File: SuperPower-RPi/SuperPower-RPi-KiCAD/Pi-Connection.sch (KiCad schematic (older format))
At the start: 1 part, among them J1 Raspberry_Pi_2_3

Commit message: Cleaned up documentation.
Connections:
- no-connect marks 21 -> 24
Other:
- note added: "Pins to STM32:\nGPIO5 to trigger update\nGPIO4 to indicate reboot/restart"
- note removed: "Pins to STM32:\nGPIO____ to trigger update\nGPIO____ to indicate reboot/restart"
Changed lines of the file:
@@
 NoConn ~ 6000 2300
 Text Notes 1200 2500 0    50   ~ 0
-Pins to STM32:\nGPIO____ to trigger update\nGPIO____ to indicate reboot/restart
+Pins to STM32:\nGPIO5 to trigger update\nGPIO4 to indicate reboot/restart
 Text HLabel 6800 3300 2    50   BiDi ~ 0
 GPIO4
@@
 Wire Wire Line
 	5000 4100 4700 4100
+NoConn ~ 5000 3800
+NoConn ~ 5000 3900
+NoConn ~ 5000 4000
 $EndSCHEMATC

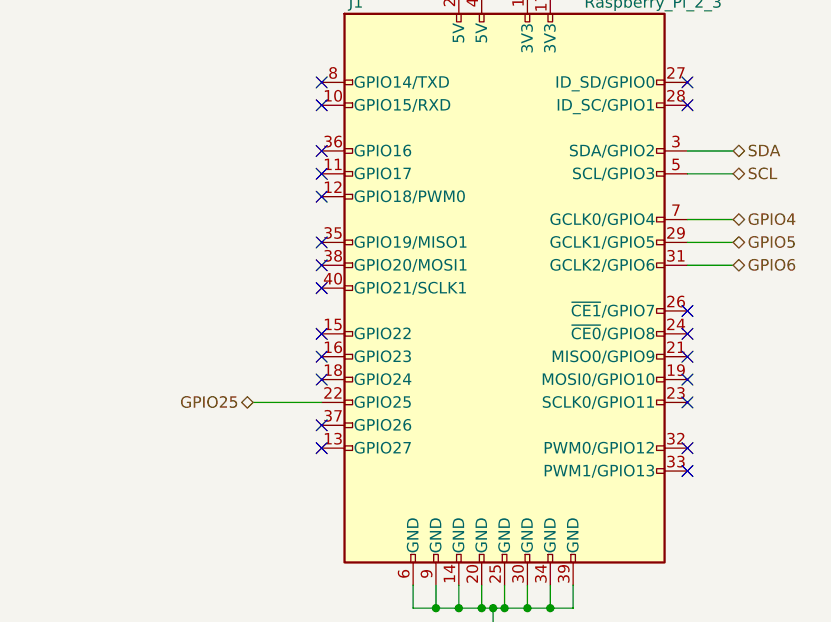
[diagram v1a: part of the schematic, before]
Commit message: Split the I2C busses and added the RPi-SWD connection.
It was found that when the RPi was powered off, the I2C connection was lost.
This was because the RPI has pull-ups on board that would act as voltage dividers.

The SWD connection to the RPi was made via jumpers to allow programming and
debugging of the STM directly via the Pi.
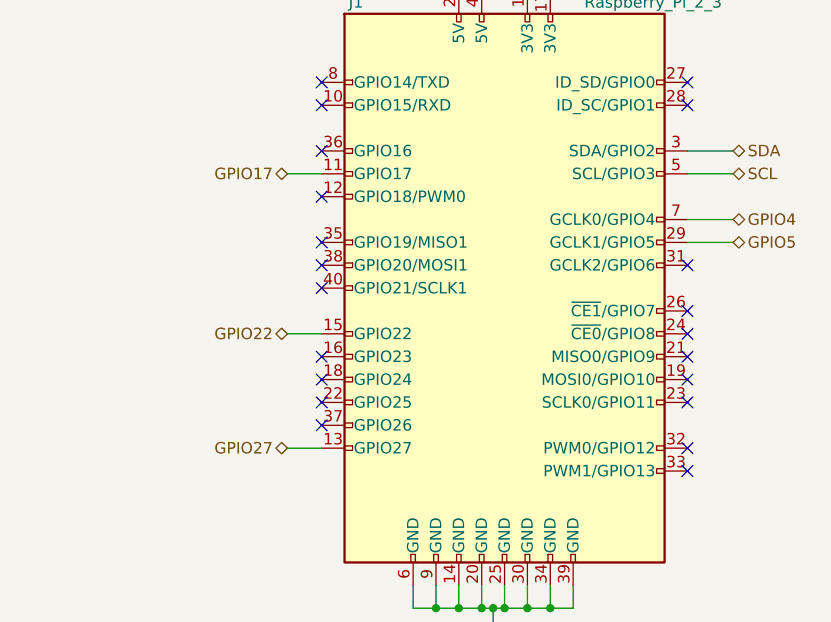
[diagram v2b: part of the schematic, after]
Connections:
- net GPIO17: now reaches J1.11 (GPIO17)
- net GPIO27: now reaches J1.13 (GPIO27)
- net GPIO22: now reaches J1.15 (GPIO22)
- net GPIO25: no longer names the net of J1.22 (GPIO25)
- net GPIO6: no longer names the net of J1.31 (GCLK2/GPIO6)
- no-connect marks 24 -> 23
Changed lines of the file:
@@
 NoConn ~ 5000 2800
 NoConn ~ 5000 3000
-NoConn ~ 5000 3100
 NoConn ~ 5000 3200
 NoConn ~ 5000 3400
@@
 NoConn ~ 5000 3600
 NoConn ~ 5000 4200
-NoConn ~ 5000 4300
 $Comp
 L power:GND #PWR09
@@
 Text HLabel 6800 3400 2    50   BiDi ~ 0
 GPIO5
-Text HLabel 6800 3500 2    50   BiDi ~ 0
-GPIO6
-Text HLabel 4700 4100 0    50   BiDi ~ 0
-GPIO25
 Wire Wire Line
 	6800 3400 6600 3400
-Wire Wire Line
-	6800 3500 6600 3500
-Wire Wire Line
-	5000 4100 4700 4100
-NoConn ~ 5000 3800
 NoConn ~ 5000 3900
 NoConn ~ 5000 4000
+NoConn ~ 5000 4100
+NoConn ~ 6600 3500
+Text HLabel 4850 3100 0    50   BiDi ~ 0
+GPIO17
+Wire Wire Line
+	4850 3100 5000 3100
+Text HLabel 4850 4300 0    50   BiDi ~ 0
+GPIO27
+Wire Wire Line
+	4850 4300 5000 4300
+Text HLabel 4850 3800 0    50   BiDi ~ 0
+GPIO22
+Wire Wire Line
+	4850 3800 5000 3800
 $EndSCHEMATC

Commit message: Updated schematic to fill out all BOM entries.
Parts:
- J1: Mfg (none) -> DNP
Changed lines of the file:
@@
 F 2 "Connector_PinSocket_2.54mm:PinSocket_2x20_P2.54mm_Vertical" H 5800 3600 50  0001 C CNN
 F 3 "https://www.raspberrypi.org/documentation/hardware/raspberrypi/schematics/rpi_SCH_3bplus_1p0_reduced.pdf" H 5800 3600 50  0001 C CNN
+F 4 "DNP" H 5800 3600 50  0001 C CNN "Mfg"
 	1    5800 3600
 	1    0    0    -1

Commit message: Updated 40-pin connector holes from 1mm to 1.2mm to allow for 1mm pogo pins.
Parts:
- J1: footprint Connector_PinSocket_2.54mm:PinSocket_2x20_P2.54mm_Vertical -> SuperPower-RPi-KiCAD:PinSocket_2x20_P2.54mm_Vertical_With_Pogo
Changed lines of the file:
@@
 F 0 "J1" H 5150 4850 50  0000 C CNN
 F 1 "Raspberry_Pi_2_3" H 6450 4850 50  0000 C CNN
-F 2 "Connector_PinSocket_2.54mm:PinSocket_2x20_P2.54mm_Vertical" H 5800 3600 50  0001 C CNN
+F 2 "SuperPower-RPi-KiCAD:PinSocket_2x20_P2.54mm_Vertical_With_Pogo" H 5800 3600 50  0001 C CNN
 F 3 "https://www.raspberrypi.org/documentation/hardware/raspberrypi/schematics/rpi_SCH_3bplus_1p0_reduced.pdf" H 5800 3600 50  0001 C CNN
 F 4 "DNP" H 5800 3600 50  0001 C CNN "Mfg"
